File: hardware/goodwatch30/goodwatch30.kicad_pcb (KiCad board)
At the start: 2 copper layers, 25.6 x 27.6 mm, 23 parts, among them J1 ANT_U.FL, U1 CC430F613x, U2 0915LP15B02, U3 B0310J50100AHF, Y1 32.768kHz, Y2 FA128 26MHz

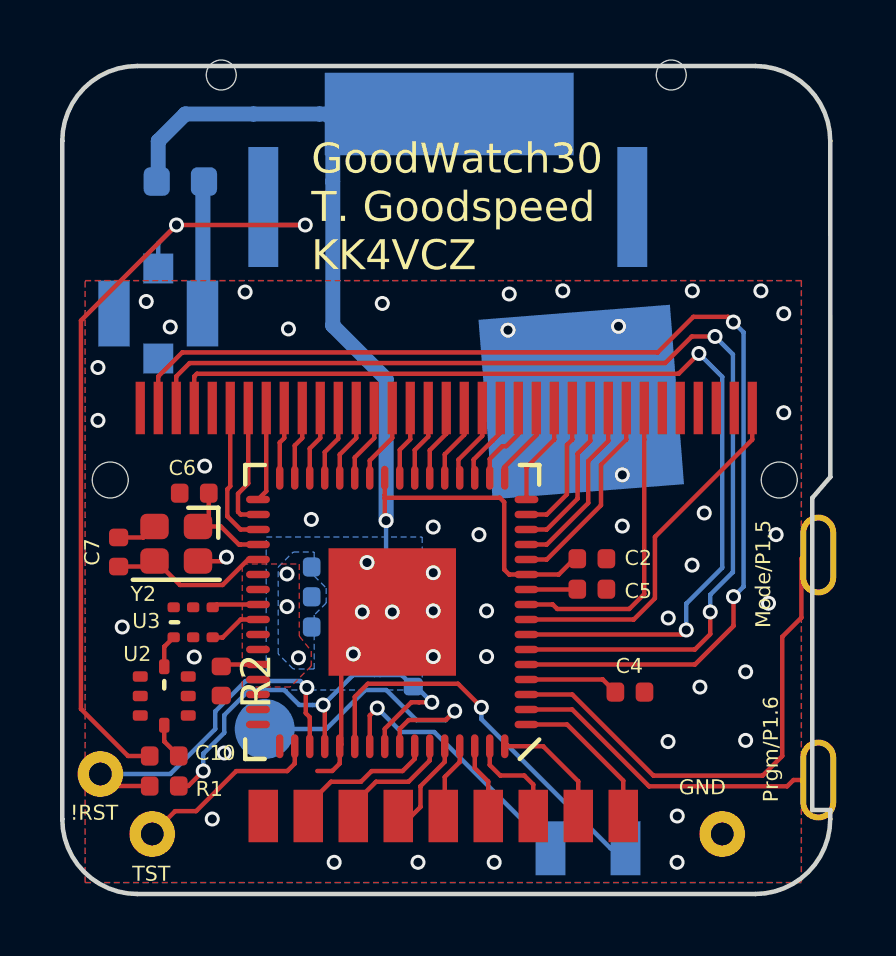
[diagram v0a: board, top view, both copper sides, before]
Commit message: Placed u.fl coax connector insight a hole of the battery pastic frame.
I replaced the 220pF block cap in front of the antenna with a cap jumper to switch between the antenna and the u.fl coax connector.
To create some space for the coax connector I modified the casio board footprint. At the footprint I moved and reshaped the spy-bi-wire pads.
Travis used clip connectors on one of the photos so I added some holes to to pads. If it is not possible to use clip connectors we could solder a 50 mil header or cable on to these pads (maybe even using a pogo pin adapter?).
The u.fl connector is placed at the approximate position of the hole in the pastic frame (this might not fit since I am still missing the accurate dimentions of the pastic frame).
I added some markings to the top silk screen to visualize the jumper settings and resized/repositioned some component markings.

The routing of VCC on the ~RST pullup (R1) is not that nice anymore.
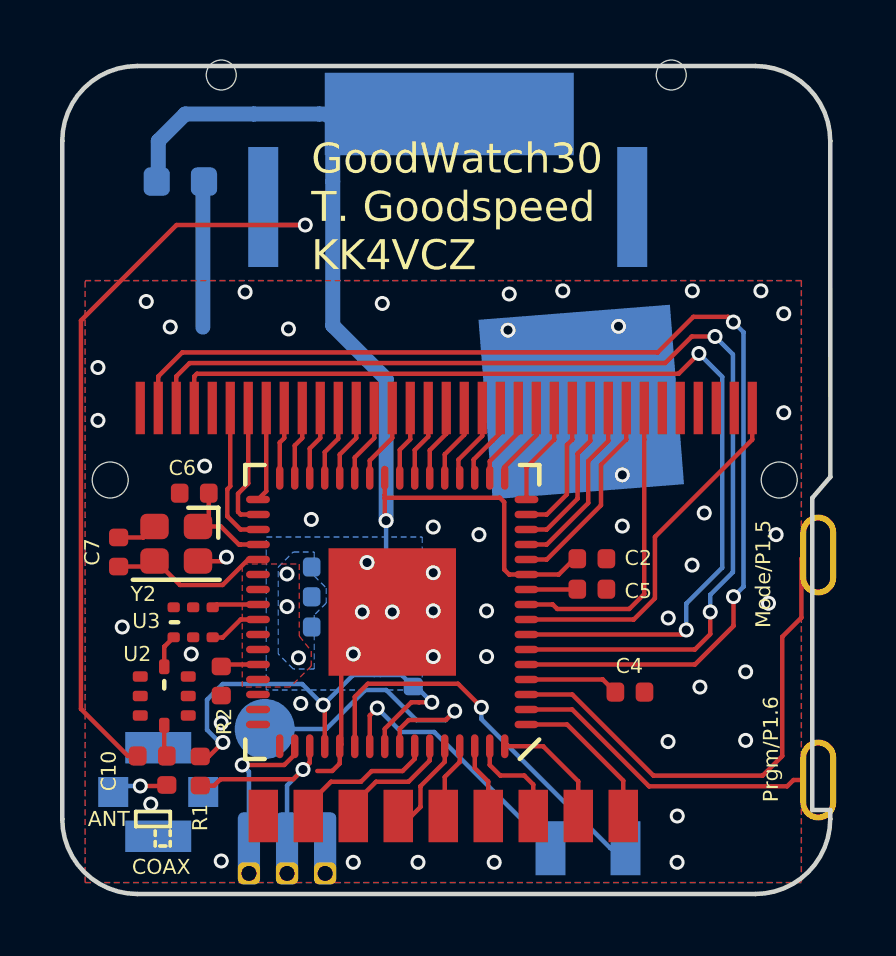
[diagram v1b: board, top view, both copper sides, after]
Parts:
- C10: footprint Capacitor_SMD:C_0402_1005Metric -> goodwatch30:C_Jumper_0402_1005Metric
- moved J1 16.0 mm to (99.8, 83.0), turned to 90 degrees
- moved R1 1.30 mm to (101.2, 82.3), turned to 270 degrees
- moved C10 0.40 mm to (99.6, 81.8), turned to 0 degrees
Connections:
- J1 pad 1: Net-(A1-Pad1) -> Net-(C10-Pad3)
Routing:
- net /!RST: track 12.5 -> 7.68 mm
- net Net-(A1-Pad1): track 28.3 -> 26.2 mm, vias 2 -> 1
- net Net-(C10-Pad3): track 0.00 -> 1.93 mm, vias 0 -> 1
- net /TST: track 6.30 -> 5.04 mm, vias 0 -> 1
- net GND: vias 49 -> 51
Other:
- board text added: "ANT"
- board text added: "BUZZ"
- board text added: "COAX"
